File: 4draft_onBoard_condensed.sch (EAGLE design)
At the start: 69 parts, among them IC3 74ABT125PW, IC4 MAX4466KS, J2 USB_MINI-B_DIGIKEY, Q1 NPN 40V 1A SOT-23

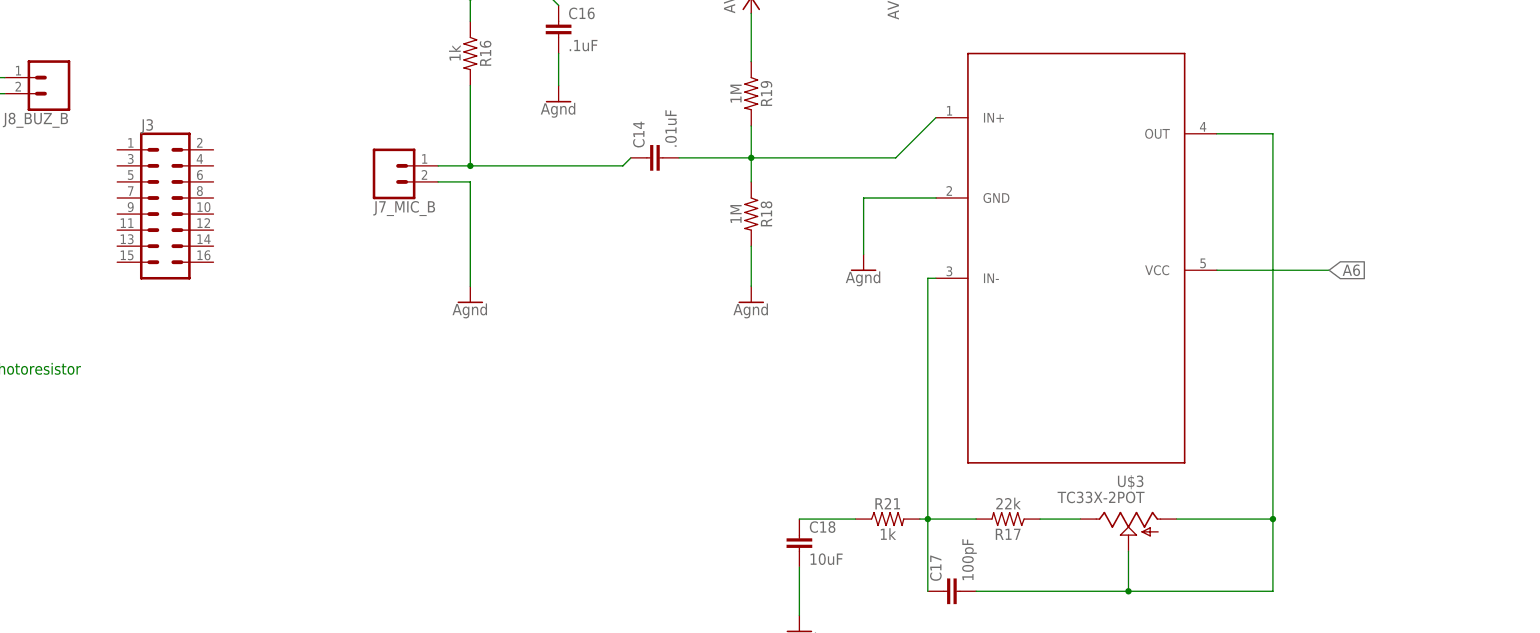
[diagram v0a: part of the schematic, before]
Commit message: re arranging nano layout
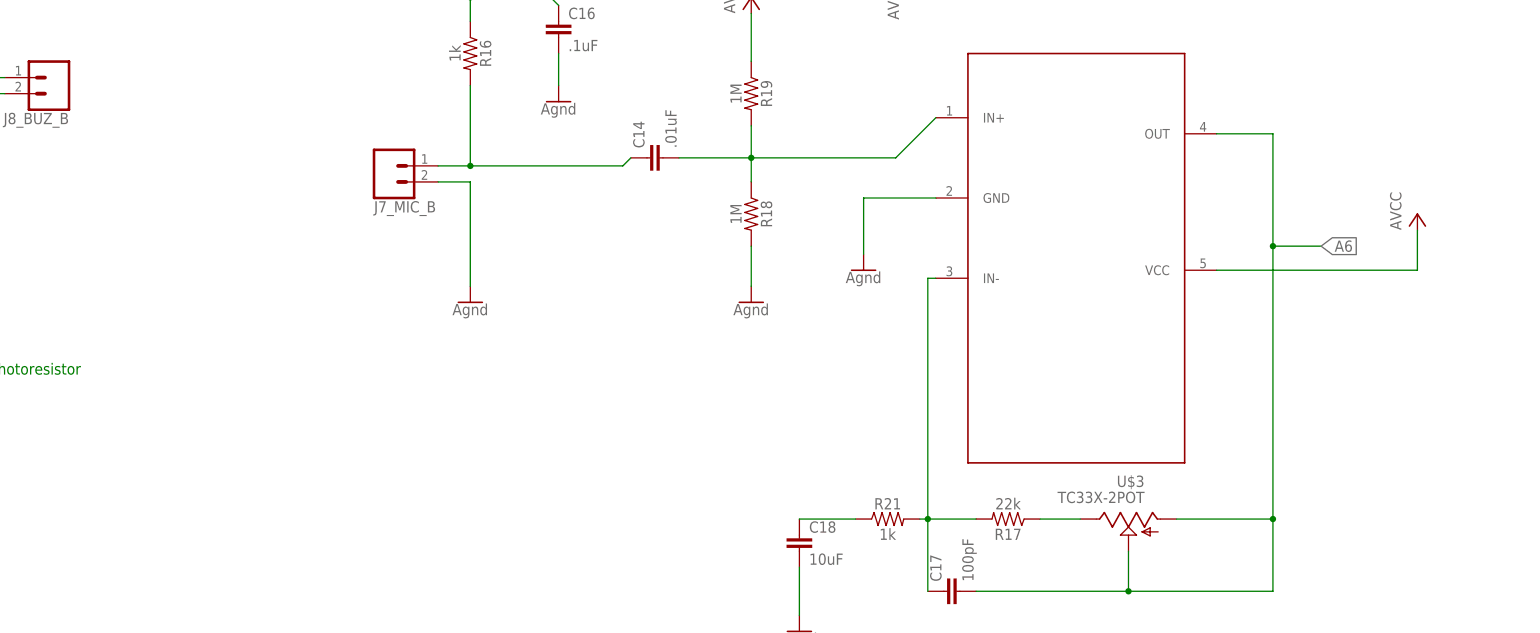
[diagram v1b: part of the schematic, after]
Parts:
- removed J3: (no value), SparkFun-Connectors:CONN_08X2
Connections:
- removed net N$32: C17.2, IC4.OUT, U$3.2, U$3.3
- removed net VCC: C11.+, FB1.2, FB3.2, FTDI231XS1.VCC, R19.1, R20.1
- new net AVCC: FB1.2, IC4.VCC, R19.1, R20.1
- net 5V: now also C11.+, FB3.2, FTDI231XS1.VCC
- net A6: now also C17.2, IC4.OUT, U$3.2, U$3.3; no longer IC4.VCC
